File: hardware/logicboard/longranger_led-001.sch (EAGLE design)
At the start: 4 parts, among them J1 LED

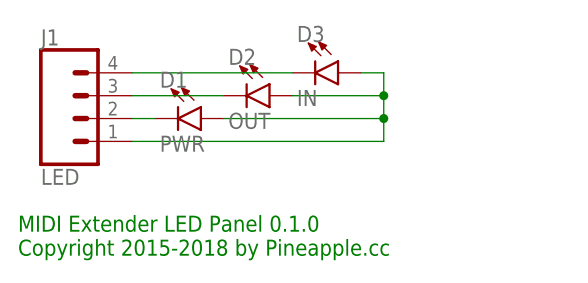
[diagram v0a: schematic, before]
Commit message: Changed layout.
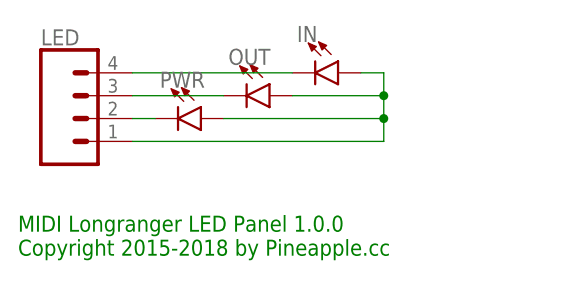
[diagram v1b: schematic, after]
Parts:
- IN: value IN -> (none)
- LED: value LED -> (none)
- OUT: value OUT -> (none)
- PWR: value PWR -> (none)
- renumbered D1 to PWR, D2 to OUT, D3 to IN, J1 to LED
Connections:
- net N$4 renamed PWR
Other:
- note added: "MIDI Longranger LED Panel 1.0.0 Copyright 2015-2018 by Pineapple.cc"
- note removed: "MIDI Extender LED Panel 0.1.0 Copyright 2015-2018 by Pineapple.cc"
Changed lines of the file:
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@@
 </classes>
 <parts>
-<part name="J1" library="SparkFun-Connectors" deviceset="CONN_04" device="JST-PTH-VERT" value="LED"/>
-<part name="D1" library="SparkFun-LED" deviceset="LED" device="3MM" value="PWR"/>
-<part name="D2" library="SparkFun-LED" deviceset="LED" device="3MM" value="OUT"/>
-<part name="D3" library="SparkFun-LED" deviceset="LED" device="3MM" value="IN"/>
+<part name="LED" library="SparkFun-Connectors" deviceset="CONN_04" device="JST-PTH-VERT"/>
+<part name="PWR" library="SparkFun-LED" deviceset="LED" device="3MM"/>
+<part name="OUT" library="SparkFun-LED" deviceset="LED" device="3MM"/>
+<part name="IN" library="SparkFun-LED" deviceset="LED" device="3MM"/>
 </parts>
 <sheets>
 <sheet>
 <plain>
-<text x="2.54" y="2.54" size="1.778" layer="91">MIDI Extender LED Panel 0.1.0
+<text x="2.54" y="2.54" size="1.778" layer="91">MIDI Longranger LED Panel 1.0.0
 Copyright 2015-2018 by Pineapple.cc</text>
 </plain>
 <instances>
-<instance part="J1" gate="G$1" x="10.16" y="17.78"/>
-<instance part="D1" gate="G$1" x="22.86" y="17.78" rot="R270"/>
-<instance part="D2" gate="G$1" x="30.48" y="20.32" rot="R270"/>
-<instance part="D3" gate="G$1" x="38.1" y="22.86" rot="R270"/>
+<instance part="LED" gate="G$1" x="10.16" y="17.78"/>
+<instance part="PWR" gate="G$1" x="22.86" y="17.78" rot="R270"/>
+<instance part="OUT" gate="G$1" x="30.48" y="20.32" rot="R270"/>
+<instance part="IN" gate="G$1" x="38.1" y="22.86" rot="R270"/>
 </instances>
 <busses>
 </busses>
 <nets>
-<net name="N$4" class="0">
+<net name="PWR" class="0">
 <segment>
-<pinref part="J1" gate="G$1" pin="1"/>
+<pinref part="LED" gate="G$1" pin="1"/>
 <wire x1="15.24" y1="15.24" x2="43.18" y2="15.24" width="0.1524" layer="91"/>
 <wire x1="43.18" y1="15.24" x2="43.18" y2="17.78" width="0.1524" layer="91"/>
-<pinref part="D3" gate="G$1" pin="A"/>
+<pinref part="IN" gate="G$1" pin="A"/>
 <wire x1="43.18" y1="17.78" x2="43.18" y2="20.32" width="0.1524" layer="91"/>
 <wire x1="43.18" y1="20.32" x2="43.18" y2="22.86" width="0.1524" layer="91"/>
 <wire x1="43.18" y1="22.86" x2="40.64" y2="22.86" width="0.1524" layer="91"/>
-<pinref part="D2" gate="G$1" pin="A"/>
+<pinref part="OUT" gate="G$1" pin="A"/>
 <wire x1="33.02" y1="20.32" x2="43.18" y2="20.32" width="0.1524" layer="91"/>
 <junction x="43.18" y="20.32"/>
-<pinref part="D1" gate="G$1" pin="A"/>
+<pinref part="PWR" gate="G$1" pin="A"/>
 <wire x1="25.4" y1="17.78" x2="43.18" y2="17.78" width="0.1524" layer="91"/>
 <junction x="43.18" y="17.78"/>
@@
 <net name="N$5" class="0">
 <segment>
-<pinref part="J1" gate="G$1" pin="2"/>
-<pinref part="D1" gate="G$1" pin="C"/>
+<pinref part="LED" gate="G$1" pin="2"/>
+<pinref part="PWR" gate="G$1" pin="C"/>
 <wire x1="17.78" y1="17.78" x2="15.24" y2="17.78" width="0.1524" layer="91"/>
 </segment>
@@
 <net name="N$11" class="0">
 <segment>
-<pinref part="J1" gate="G$1" pin="3"/>
-<pinref part="D2" gate="G$1" pin="C"/>
+<pinref part="LED" gate="G$1" pin="3"/>
+<pinref part="OUT" gate="G$1" pin="C"/>
 <wire x1="25.4" y1="20.32" x2="15.24" y2="20.32" width="0.1524" layer="91"/>
 </segment>
@@
 <net name="N$12" class="0">
 <segment>
-<pinref part="J1" gate="G$1" pin="4"/>
-<pinref part="D3" gate="G$1" pin="C"/>
+<pinref part="LED" gate="G$1" pin="4"/>
+<pinref part="IN" gate="G$1" pin="C"/>
 <wire x1="33.02" y1="22.86" x2="15.24" y2="22.86" width="0.1524" layer="91"/>
 </segment>

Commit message: Changed LED pitch.
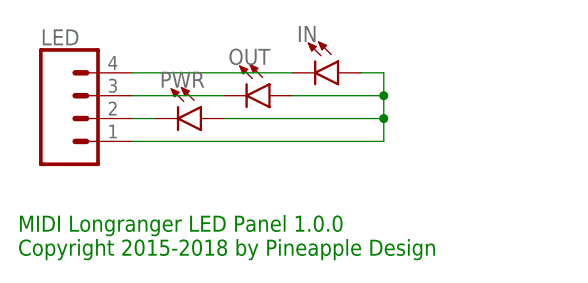
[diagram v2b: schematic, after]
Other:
- note added: "MIDI Longranger LED Panel 1.0.0 Copyright 2015-2018 by Pineapple Design"
- note removed: "MIDI Longranger LED Panel 1.0.0 Copyright 2015-2018 by Pineapple.cc"
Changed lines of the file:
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@@
 </variantdefs>
 <classes>
-<class number="0" name="default" width="0" drill="0">
+<class number="0" name="default" width="0.127" drill="0.127">
+<clearance class="0" value="0.127"/>
 </class>
 </classes>
@@
 <plain>
 <text x="2.54" y="2.54" size="1.778" layer="91">MIDI Longranger LED Panel 1.0.0
-Copyright 2015-2018 by Pineapple.cc</text>
+Copyright 2015-2018 by Pineapple Design</text>
 </plain>
 <instances>
